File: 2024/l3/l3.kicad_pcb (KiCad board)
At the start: 2 copper layers, 137.5 x 129.1 mm, 23 parts, among them J1 Conn_01x04, SW1 SW_SPDT, SW2 SW_SPDT, SW3 SW_SPDT, SW4 SW_SPDT, U4 DEV-15583

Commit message: remove trace test
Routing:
- net +5V: track 304.9 -> 241.3 mm
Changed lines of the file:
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@@
-	)
-	(segment
-		(start 111.4 44.07)
-		(end 156.38 89.05)
-		(width 0.5)
-		(layer "B.Cu")
-		(net 3)
 	)
 	(segment

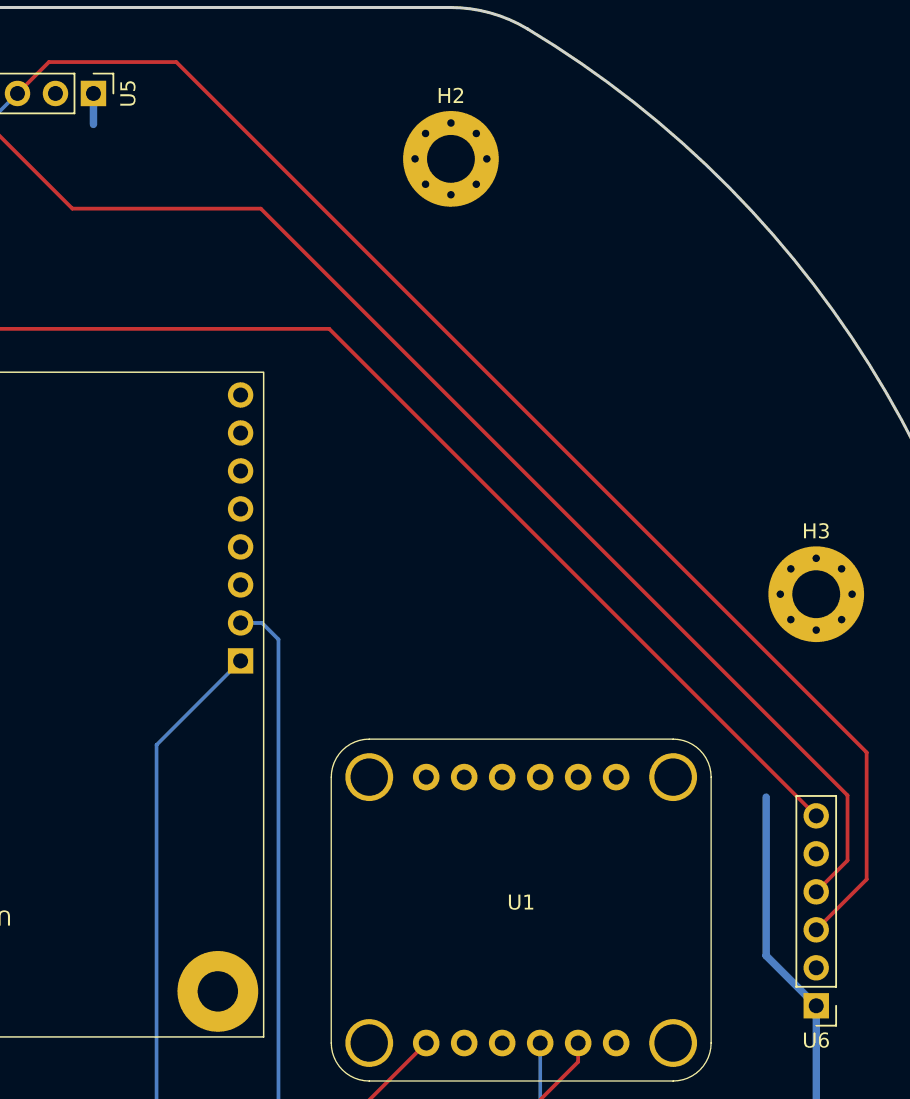
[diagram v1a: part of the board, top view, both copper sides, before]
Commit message: replace trace test
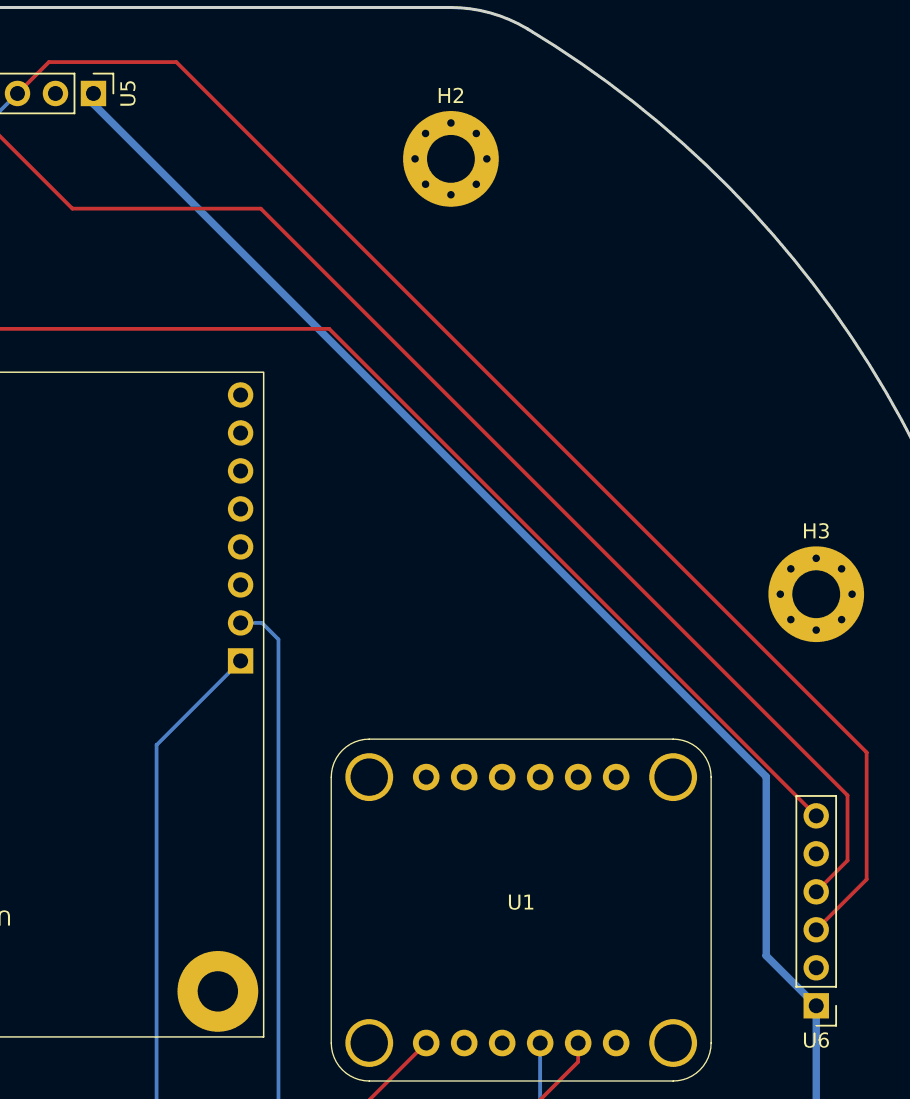
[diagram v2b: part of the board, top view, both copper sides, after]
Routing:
- net +5V: track 241.3 -> 304.9 mm
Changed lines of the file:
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@@
-	)
-	(segment
-		(start 156.38 99.654117)
-		(end 159.728431 103.002548)
-		(width 0.5)
-		(layer "B.Cu")
-		(net 3)
 	)
 	(segment
@@
 	)
 	(segment
-		(start 156.38 89.05)
-		(end 156.38 99.654117)
+		(start 156.38 87.68107)
+		(end 111.4 42.70107)
 		(width 0.5)
 		(layer "B.Cu")
@@
 	)
 	(segment
-		(start 111.4 41.999548)
-		(end 111.4 44.07)
-		(width 0.5)
-		(layer "B.Cu")
-		(net 3)
-	)
-	(segment
 		(start 136.23 137.76)
 		(end 111.43 162.56)
@@
 	)
 	(segment
+		(start 156.38 99.654117)
+		(end 156.38 87.68107)
+		(width 0.5)
+		(layer "B.Cu")
+		(net 3)
+	)
+	(segment
+		(start 111.4 42.70107)
+		(end 111.4 41.999548)
+		(width 0.5)
+		(layer "B.Cu")
+		(net 3)
+	)
+	(segment
 		(start 59.07 126.26)
 		(end 66.85 126.26)
 		(width 0.5)
 		(layer "B.Cu")
+		(net 3)
+	)
+	(segment
+		(start 159.728431 103.002548)
+		(end 156.38 99.654117)
+		(width 0.5)
+		(layer "B.Cu")

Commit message: another test
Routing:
- net /SDAToF: track 281.1 -> 225.6 mm
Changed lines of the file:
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@@
-	)
-	(segment
-		(start 161.82 88.93)
-		(end 122.59 49.7)
-		(width 0.25)
-		(layer "F.Cu")
-		(net 5)
 	)
 	(segment

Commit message: add back trace
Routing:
- net /SDAToF: track 225.6 -> 291.3 mm
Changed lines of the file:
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@@
+	)
+	(segment
+		(start 122.59 49.7)
+		(end 112.358751 49.7)
+		(width 0.25)
+		(layer "F.Cu")
+		(net 5)
 	)
 	(segment
@@
 		(width 0.25)
 		(layer "F.Cu")
+		(net 5)
+	)
+	(segment
+		(start 122.59 49.7)
+		(end 161.82 88.93)
+		(width 0.25)
+		(layer "F.Cu")

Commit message: PCB_done
Rearrange traces
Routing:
- net /SDAToF: track 291.3 -> 289.0 mm
- net /SCLToF: track 272.7 -> 273.3 mm
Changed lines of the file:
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@@
+	)
+	(segment
+		(start 56.01 99.78)
+		(end 56.07 99.72)
+		(width 0.5)
+		(layer "F.Cu")
+		(net 3)
 	)
 	(segment
@@
 	)
 	(segment
-		(start 54.59 107.69)
-		(end 54.68 107.78)
-		(width 0.5)
-		(layer "F.Cu")
-		(net 3)
-	)
-	(segment
-		(start 54.59 99.99)
-		(end 54.59 107.69)
-		(width 0.5)
-		(layer "F.Cu")
-		(net 3)
-	)
-	(segment
-		(start 54.61 99.97)
-		(end 54.59 99.99)
+		(start 55.99 108.07)
+		(end 56.01 108.05)
+		(width 0.5)
+		(layer "F.Cu")
+		(net 3)
+	)
+	(segment
+		(start 56.01 108.05)
+		(end 56.01 99.78)
 		(width 0.5)
 		(layer "F.Cu")
@@
 	)
 	(via
-		(at 54.61 99.97)
+		(at 56.07 99.72)
 		(size 0.8)
 		(drill 0.4)
@@
 	)
 	(via
-		(at 54.68 107.78)
+		(at 55.99 108.07)
 		(size 0.8)
 		(drill 0.4)
@@
 	)
 	(segment
-		(start 54.62 99.96)
-		(end 54.62 92.06)
+		(start 55.99 108.07)
+		(end 55.98 108.08)
+		(width 0.5)
+		(layer "B.Cu")
+		(net 3)
+	)
+	(segment
+		(start 56.02 99.67)
+		(end 56.02 93.46)
 		(width 0.5)
 		(layer "B.Cu")
@@
 	)
 	(segment
-		(start 54.62 92.06)
-		(end 52.762548 90.202548)
-		(width 0.5)
-		(layer "B.Cu")
-		(net 3)
-	)
-	(segment
 		(start 159.728431 103.002548)
 		(end 159.728431 110.056569)
@@
 	)
 	(segment
+		(start 52.762548 90.202548)
+		(end 50.271569 90.202548)
+		(width 0.5)
+		(layer "B.Cu")
+		(net 3)
+	)
+	(segment
 		(start 98.6 159.602548)
 		(end 94.902548 159.602548)
@@
 	)
 	(segment
-		(start 54.61 99.97)
-		(end 54.62 99.96)
+		(start 55.98 108.08)
+		(end 55.98 123.17)
 		(width 0.5)
 		(layer "B.Cu")
@@
 	)
 	(segment
-		(start 54.68 107.78)
-		(end 54.68 121.87)
-		(width 0.5)
-		(layer "B.Cu")
-		(net 3)
-	)
-	(segment
 		(start 72.34 137.04)
 		(end 66.85 137.04)
@@
 	)
 	(segment
-		(start 54.68 121.87)
-		(end 59.07 126.26)
-		(width 0.5)
-		(layer "B.Cu")
-		(net 3)
-	)
-	(segment
 		(start 66.85 137.04)
 		(end 59.07 137.04)
@@
 	)
 	(segment
+		(start 56.07 99.72)
+		(end 56.02 99.67)
+		(width 0.5)
+		(layer "B.Cu")
+		(net 3)
+	)
+	(segment
 		(start 59.07 126.26)
 		(end 66.85 126.26)
@@
 	)
 	(segment
-		(start 52.762548 90.202548)
-		(end 50.271569 90.202548)
+		(start 55.98 123.17)
+		(end 59.07 126.26)
 		(width 0.5)
 		(layer "B.Cu")
@@
 		(start 56.5 134.47)
 		(end 56.5 128.83)
+		(width 0.5)
+		(layer "B.Cu")
+		(net 3)
+	)
+	(segment
+		(start 56.02 93.46)
+		(end 52.762548 90.202548)
 		(width 0.5)
 		(layer "B.Cu")
@@
 	)
 	(segment
-		(start 55.84 135.07)
-		(end 55.19 135.72)
+		(start 54.85 136.71)
+		(end 54.85 103.02)
+		(width 0.25)
+		(layer "F.Cu")
+		(net 5)
+	)
+	(segment
+		(start 98.097452 151.48)
+		(end 69.62 151.48)
 		(width 0.25)
 		(layer "F.Cu")
@@
 	)
 	(segment
-		(start 76.17 156.7)
-		(end 103.317452 156.7)
-		(width 0.25)
-		(layer "F.Cu")
-		(net 5)
-	)
-	(segment
-		(start 54.692548 97.822548)
-		(end 55.84 98.97)
+		(start 106.22 159.602548)
+		(end 98.097452 151.48)
+		(width 0.25)
+		(layer "F.Cu")
+		(net 5)
+	)
+	(segment
+		(start 54.85 103.02)
+		(end 50.271569 98.441569)
+		(width 0.25)
+		(layer "F.Cu")
+		(net 5)
+	)
+	(segment
+		(start 50.271569 98.441569)
+		(end 50.271569 97.822548)
 		(width 0.25)
 		(layer "F.Cu")
@@
 	)
 	(segment
-		(start 50.271569 97.822548)
-		(end 54.692548 97.822548)
-		(width 0.25)
-		(layer "F.Cu")
-		(net 5)
-	)
-	(segment
-		(start 55.84 98.97)
-		(end 55.84 135.07)
-		(width 0.25)
-		(layer "F.Cu")
-		(net 5)
-	)
-	(segment
-		(start 55.19 135.72)
-		(end 76.17 156.7)
+		(start 69.62 151.48)
+		(end 54.85 136.71)
 		(width 0.25)
 		(layer "F.Cu")
@@
 	)
 	(segment
-		(start 103.317452 156.7)
-		(end 106.22 159.602548)
-		(width 0.25)
-		(layer "F.Cu")
-		(net 5)
-	)
-	(segment
 		(start 161.82 93.290979)
 		(end 161.82 88.93)
@@
 	)
 	(segment
-		(start 163.1 86.06)
-		(end 116.94 39.9)
-		(width 0.25)
-		(layer "F.Cu")
-		(net 6)
-	)
-	(segment
 		(start 163.1 94.550979)
 		(end 163.1 86.06)
@@
 	)
 	(segment
+		(start 116.28 39.24)
+		(end 109.079548 39.24)
+		(width 0.25)
+		(layer "F.Cu")
+		(net 6)
+	)
+	(segment
+		(start 50.406617 95.1475)
+		(end 50.271569 95.282548)
+		(width 0.25)
+		(layer "F.Cu")
+		(net 6)
+	)
+	(segment
+		(start 109.079548 39.24)
+		(end 106.32 41.999548)
+		(width 0.25)
+		(layer "F.Cu")
+		(net 6)
+	)
+	(segment
+		(start 63.095235 79.324765)
+		(end 65.577642 76.842358)
+		(width 0.25)
+		(layer "F.Cu")
+		(net 6)
+	)
+	(segment
+		(start 65.577642 76.842358)
+		(end 65.577642 76.600256)
+		(width 0.25)
+		(layer "F.Cu")
+		(net 6)
+	)
+	(segment
+		(start 163.1 86.06)
+		(end 116.28 39.24)
+		(width 0.25)
+		(layer "F.Cu")
+		(net 6)
+	)
+	(segment
 		(start 159.728431 97.922548)
 		(end 163.1 94.550979)
 		(width 0.25)
 		(layer "F.Cu")
-		(net 6)
-	)
-	(segment
-		(start 50.406617 95.1475)
-		(end 50.271569 95.282548)
-		(width 0.25)
-		(layer "F.Cu")
-		(net 6)
-	)
-	(segment
-		(start 63.095235 79.324765)
-		(end 65.577642 76.842358)
-		(width 0.25)
-		(layer "F.Cu")
-		(net 6)
-	)
-	(segment
-		(start 65.577642 76.842358)
-		(end 65.577642 76.600256)
-		(width 0.25)
-		(layer "F.Cu")
-		(net 6)
-	)
-	(segment
-		(start 108.419548 39.9)
-		(end 106.32 41.999548)
-		(width 0.25)
-		(layer "F.Cu")
-		(net 6)
-	)
-	(segment
-		(start 116.94 39.9)
-		(end 108.419548 39.9)
-		(width 0.25)
-		(layer "F.Cu")
